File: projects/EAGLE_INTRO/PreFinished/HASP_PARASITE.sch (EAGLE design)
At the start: 5 parts

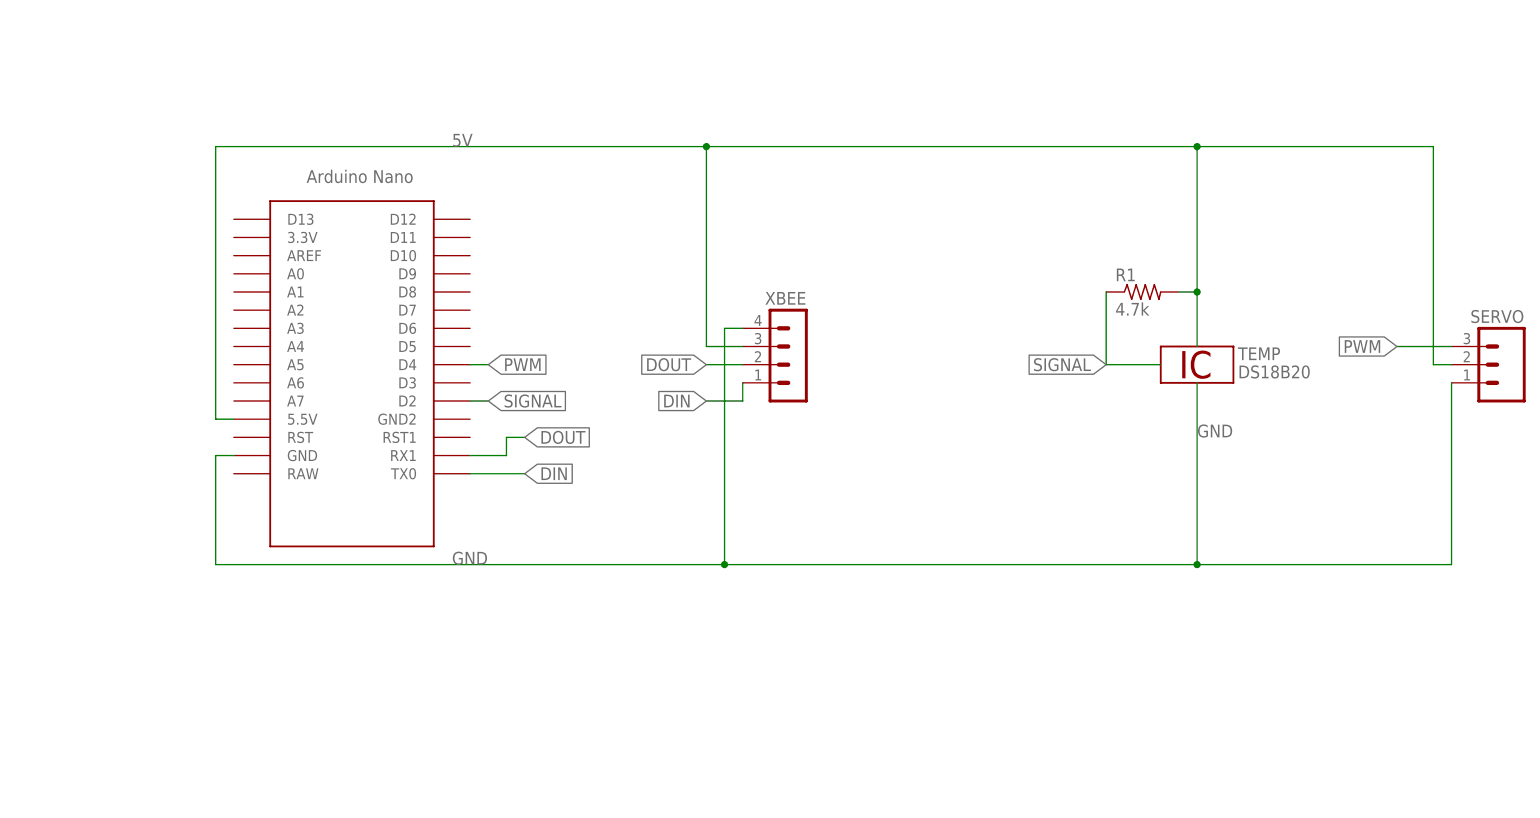
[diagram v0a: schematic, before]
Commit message: Added edits to teensy 3.6 schematic for the plantower. Added stuff from EAGLE intro presentation.
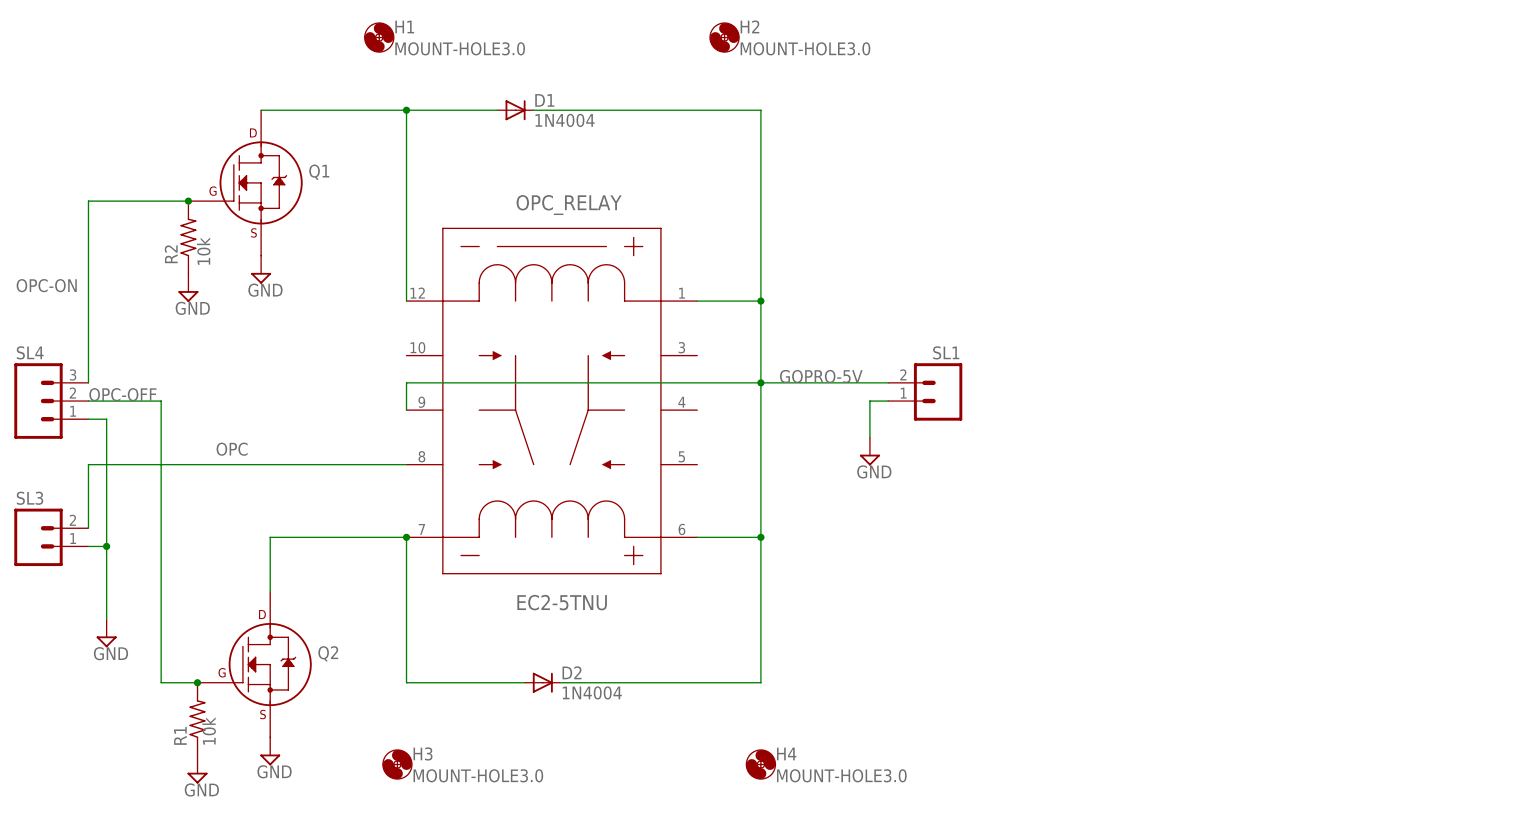
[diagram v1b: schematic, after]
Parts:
- removed SERVO: (no value), con-amp-quick:M03
- removed TEMP: DS18B20, 1wire:DS18B20
- removed U$1: NANO, Arduino-clone:NANO
- removed XBEE: (no value), con-lstb:MA04-1
- added D1, D2: 1N4004, diode:1N4004
- added H1, H2, H3, H4: MOUNT-HOLE3.0, holes:MOUNT-HOLE3.0
- added OPC_RELAY: EC2-5TNU, EC2-5TNU:EC2-5TNU
- added Q1, Q2: (no value), transistors:2N7000_TO92
- added R2: (no value), rcl:R-US_0207/7
- added SL1, SL3: (no value), con-amp-quick:M02
- added SL4: (no value), con-amp-quick:M03
- R1: value 4.7k -> (none); device resistor:R-US_0204/7 -> rcl:R-US_0207/7
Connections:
- removed net 5V: R1.2, SERVO.2, U$1.5.5V, XBEE.3
- removed net DIN: U$1.TX0, XBEE.1
- removed net DOUT: U$1.RX1, XBEE.2
- removed net PWM: SERVO.3, U$1.D4
- removed net SIGNAL: R1.1, U$1.D2
- new net GOPRO-5V: D1.C, D2.C, OPC_RELAY.1, OPC_RELAY.5, OPC_RELAY.8, SL1.2
- new net N$1: D1.A, OPC_RELAY.10, Q1.D
- new net N$3: D2.A, OPC_RELAY.6, Q2.D
- new net OPC: OPC_RELAY.7, SL3.2
- new net OPC-OFF: Q2.G, R1.2, SL4.2
- new net OPC-ON: Q1.G, R2.2, SL4.3
- net GND: now also Q1.S, Q2.S, R1.1, R2.1, SL1.1, SL3.1, SL4.1; no longer SERVO.1, U$1.GND, XBEE.4
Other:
- note added: "10k"
- moved on the sheet: R1
